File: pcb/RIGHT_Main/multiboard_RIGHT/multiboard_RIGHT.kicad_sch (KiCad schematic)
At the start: 134 parts, among them J1 OLED, SW13 SW_Push, SW14 SW_Push, SW15 SW_Push, SW16 SW_Push, SW17 SW_Push, SW18 SW_Push, SW19 SW_Push, SW20 SW_Push, SW21 SW_Push, SW22 SW_Push, SW23 SW_Push, SW24 SW_Push, SW25 SW_Push, SW26 SW_Push, SW27 SW_Push, SW28 SW_Push, SW29 SW_Push, SW3 SW_Push, SW30 SW_Push, SW31 SW_Push, SW32 SW_Push, SW33 SW_Push, SW34 SW_Push, SW35 SW_Push, SW36 SW_Push, SW37 SW_Push, SW38 SW_Push, SW39 SW_Push, SW4 SW_Push, SW40 SW_Push, SW41 SW_Push, SW42 SW_Push, SW43 SW_Push, SW44 SW_Push, SW45 SW_Push, SW46 SW_Push, SW47 SW_Push, SW48 SW_Push, SW49 SW_Push, SW5 SW_Push, SW50 SW_Push, SW51 SW_Push, SW52 SW_Push, SW53 SW_Push, SW54 SW_Push, SW55 SW_Push, SW56 SW_Push, SW57 SW_Push, SW58 SW_Push, SW59 SW_Push, SW6 SW_Push, SW60 SW_Push, SW61 SW_Push, SW62 SW_Push, SW63 SW_Push, SW64 SW_Push, SW65 SW_Push, SW66 SW_Push, SW67 SW_Push, SW69 SW_Push, SW7 SW_Push, SW70 SW_Push, SW71 SW_Push, SW72 SW_Push, SW73 SW_Push, SW8 SW_Push, U1 ESP32-S3-DEVKITC-1-N8R2

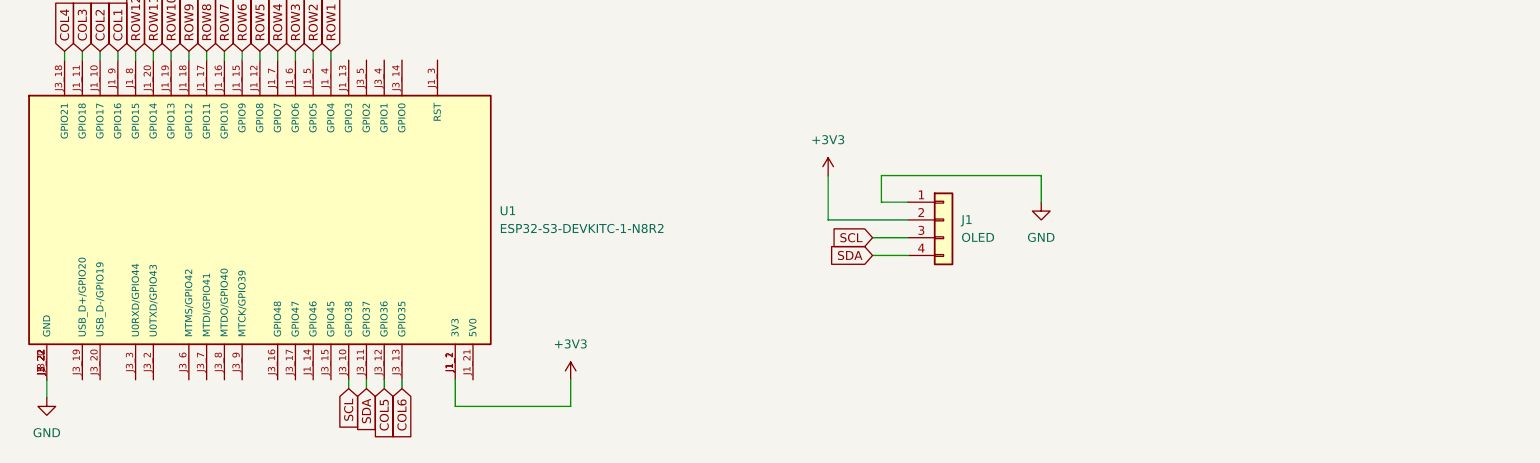
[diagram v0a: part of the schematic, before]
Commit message: add headphone jack
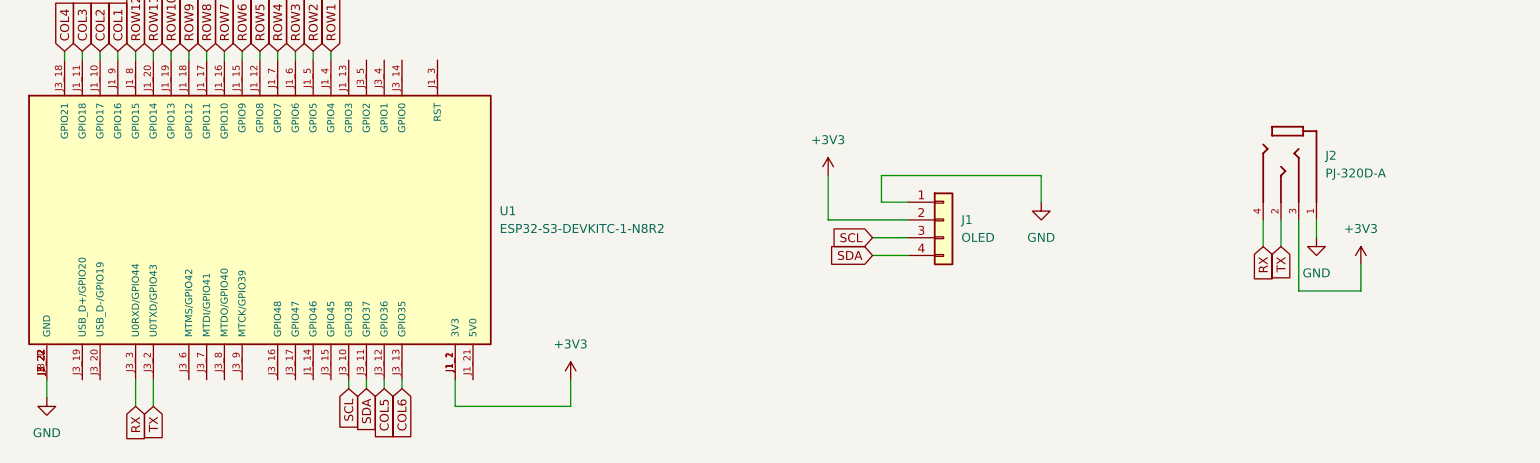
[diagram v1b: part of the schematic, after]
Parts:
- added J2: PJ-320D-A, PJ:HRO_PJ-320D-A, symbol PJ:PJ-320D-A
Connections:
- net +3V3: now also J2.3
- net GND: now also J2.1
- net TX: now reaches U1.J3_2 (U0TXD/GPIO43)
- net TX: now also J2.2
- net RX: now reaches U1.J3_3 (U0RXD/GPIO44)
- net RX: now also J2.4
